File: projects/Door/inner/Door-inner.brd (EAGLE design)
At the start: 80 x 53.3 mm, 28 parts, among them IC1 7815TV, J2 AVR_SPI_PROG_3X2PTH, J3 LCD, U2 LP2985-33DBVR, X1 POWERSUPPLY_DC21MMX, Y1 16MHz

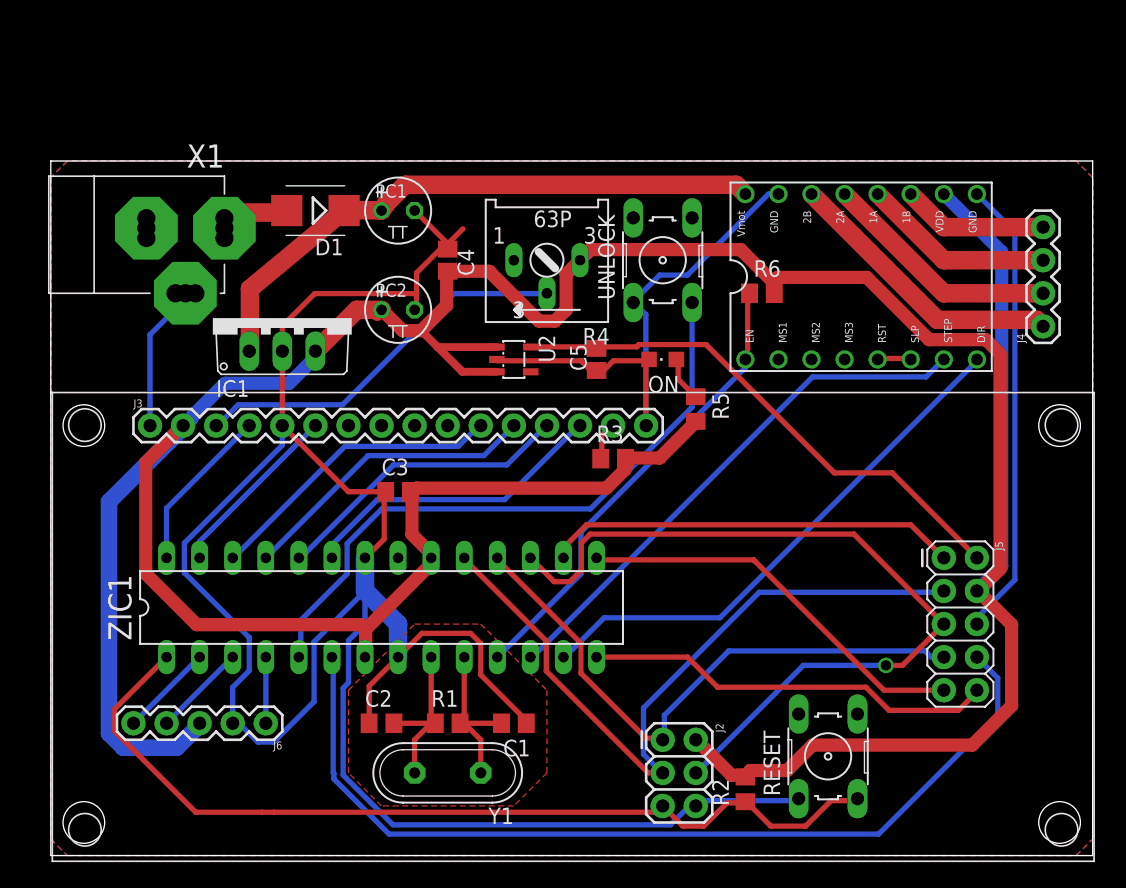
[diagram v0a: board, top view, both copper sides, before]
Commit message: Rerouted door boards for rivet-plated vias instead of plated through-holes
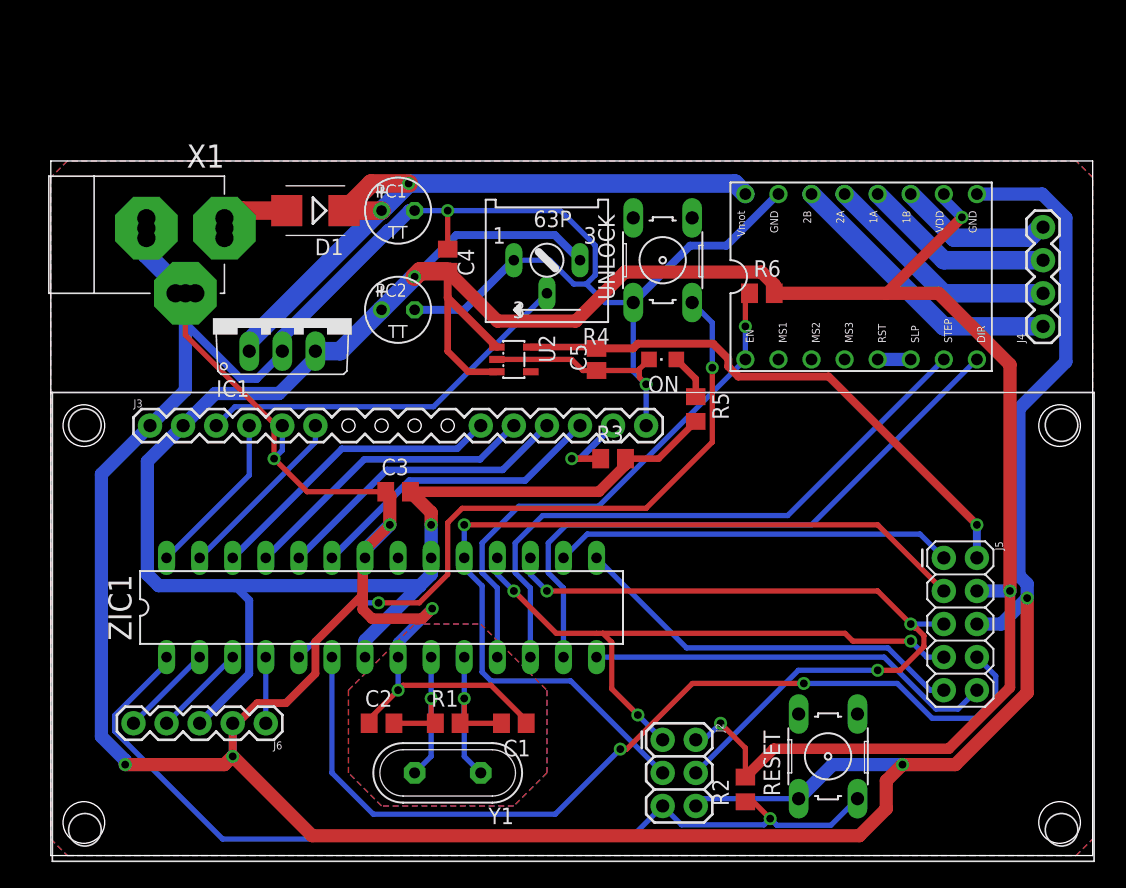
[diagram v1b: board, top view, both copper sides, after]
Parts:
- J3: value LCD -> LCD_4PINNOPADS; device lcd:LCD-16X2 -> lcd:LCD-16X2-NOPADS
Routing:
- net GND: track 264.0 -> 388.1 mm, vias 0 -> 10
- net +5V: track 289.1 -> 260.7 mm, vias 0 -> 5
- net SCK: track 55.9 -> 67.9 mm, vias 0 -> 1
- net M-STP: track 41.2 -> 48.0 mm
- net M-DIR: track 41.3 -> 48.0 mm
- net VIN: track 46.2 -> 52.9 mm, vias 0 -> 1
- net MOSI: track 64.0 -> 58.4 mm, vias 1 -> 3
- net M-EN: track 36.0 -> 40.5 mm, vias 0 -> 1
- net N$4: track 3.29 -> 6.45 mm, vias 0 -> 1
- net N$12: track 49.2 -> 52.3 mm, vias 0 -> 2
- net RESET: track 70.3 -> 73.2 mm, vias 0 -> 1
- net MISO: track 45.6 -> 48.3 mm, vias 0 -> 3
- net XTAL2: track 12.7 -> 14.6 mm, vias 0 -> 1
- net XTAL1: track 12.7 -> 14.6 mm, vias 0 -> 1
- net +3V3: track 41.3 -> 43.1 mm, vias 0 -> 1
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
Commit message: Via rivets apparently have a 0.6mm INNER diameter
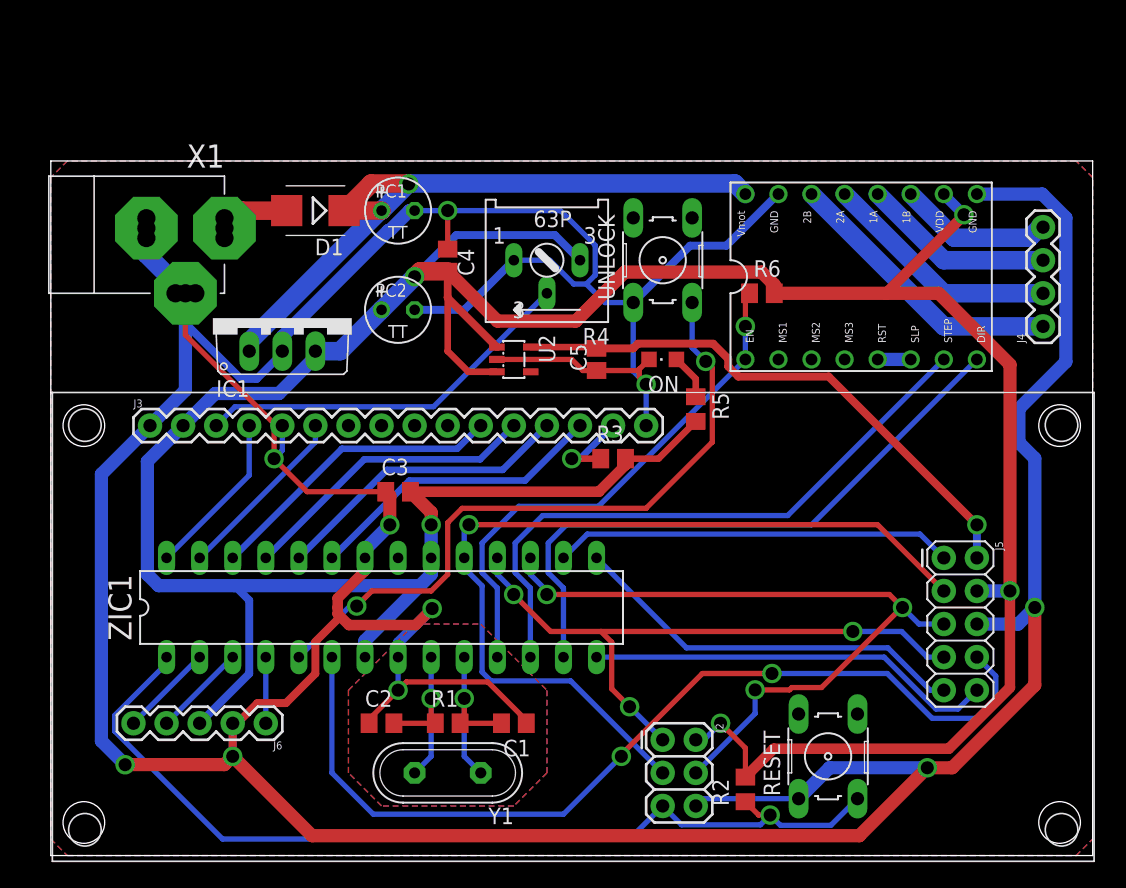
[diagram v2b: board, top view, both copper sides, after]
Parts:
- J3: value LCD_4PINNOPADS -> LCD_4PIN; device lcd:LCD-16X2-NOPADS -> lcd:LCD-16X2
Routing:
- net MOSI: track 58.4 -> 57.0 mm
- net STATUS: track 70.8 -> 71.6 mm

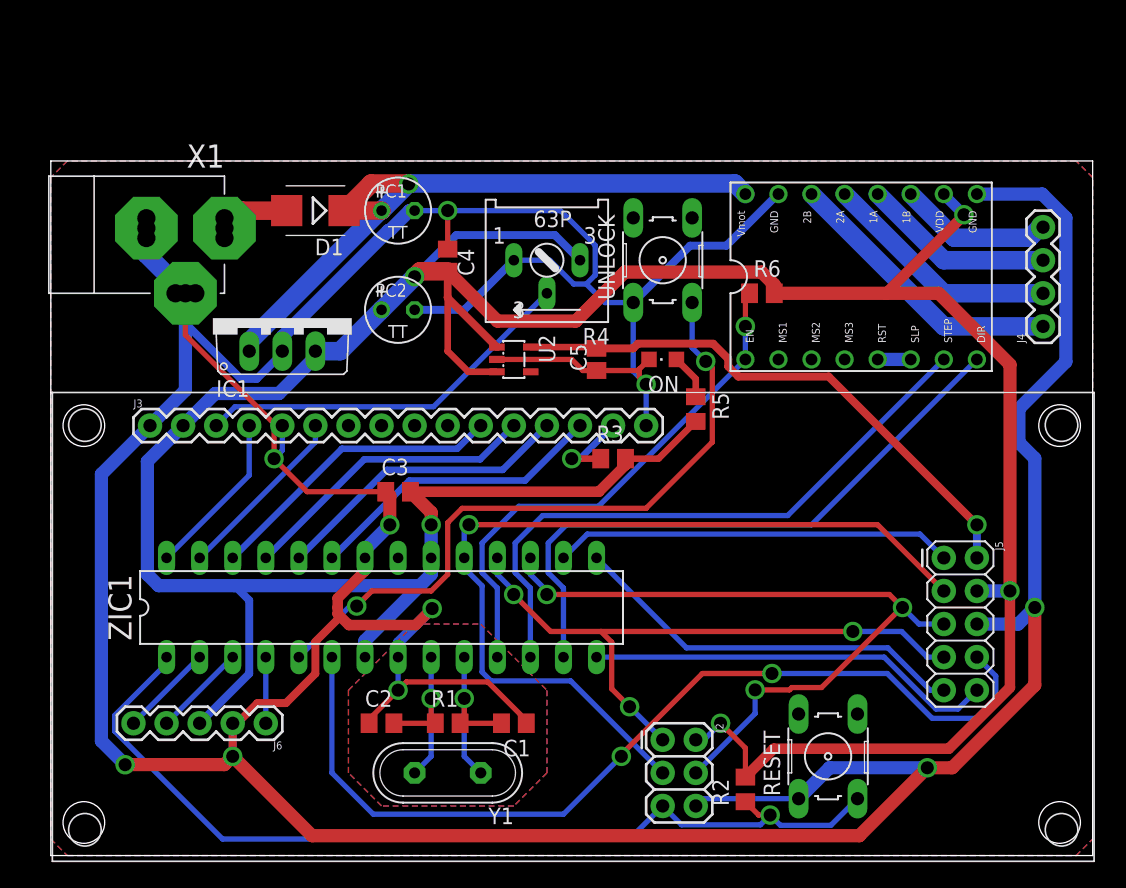
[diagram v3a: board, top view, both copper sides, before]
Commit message: Door-inner redesign
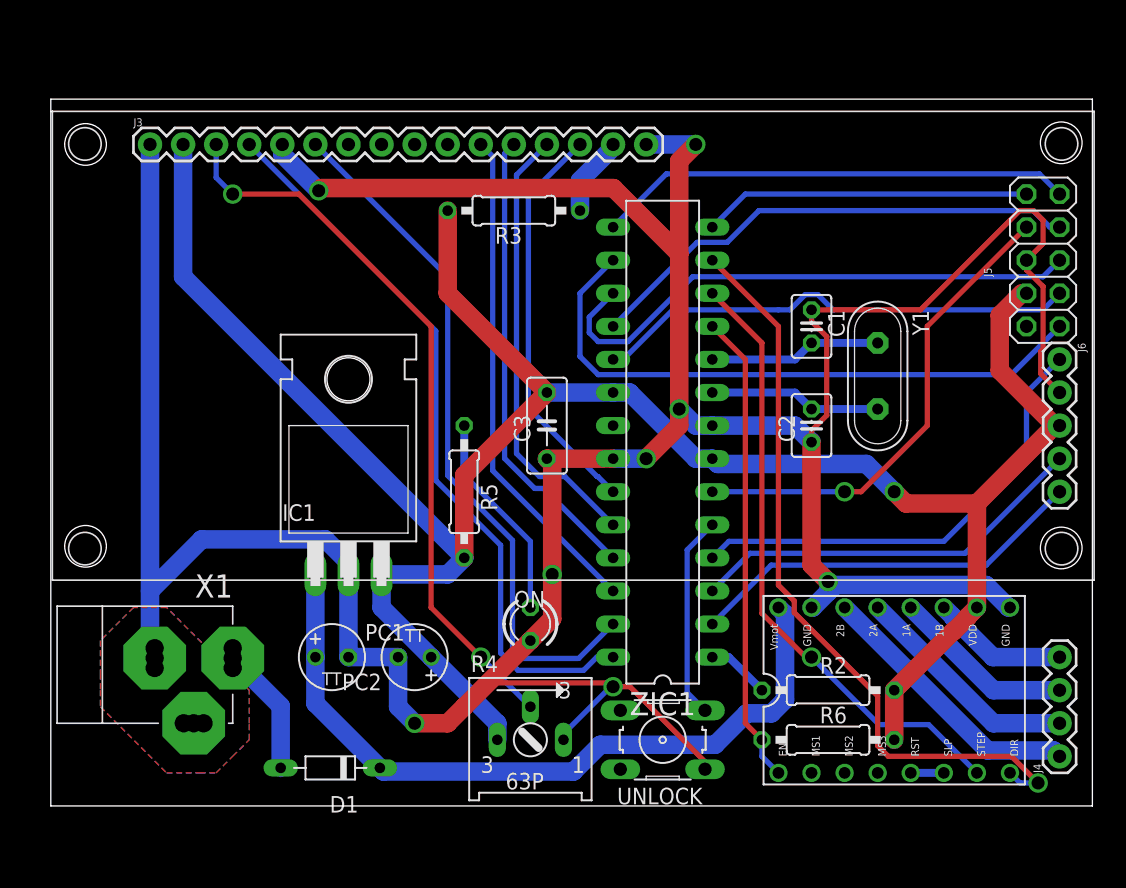
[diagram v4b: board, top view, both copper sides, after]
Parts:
- removed C4: 100n, SmartPrj:C0805
- removed C5: 1u, SmartPrj:C0805
- removed J2: AVR_SPI_PROG_3X2PTH, SparkFun-Connectors:2X3
- removed R1: 1M, resistor:R0805
- removed RESET: (no value), switch-omron:B3F-10XX
- removed U2: LP2985-33DBVR, texas:SOT23-DBV
- C1, C2: device resistor:C0805 -> resistor:C025-030X050
- C3: device resistor:C0805 -> resistor:C050-030X075
- D1: device diode:SMB -> diode:D-7.5
- IC1: value 7815TV -> 7815T; device linear:TO220V -> linear:TO220H
- J5: device SparkFun-Connectors:2X5 -> pinhead:2X05
- ON: device led:CHIPLED_0805 -> led:LED3MM
- R2, R3, R5, R6: device resistor:R0805 -> resistor:0207/10
- moved J6 67.1 mm to (77.5, 31.8), turned to 270 degrees
- moved Y1 44.9 mm to (63.5, 30.5), turned to 270 degrees
- moved D1 42.8 mm to (21.5, 0.38)
- moved C2 40.2 mm to (58.4, 26.7), turned to 90 degrees
- moved C1 38.1 mm to (58.4, 34.3), turned to 270 degrees
- moved R4 36.9 mm to (36.8, 2.54), turned to 0 degrees
- moved UNLOCK 36.8 mm to (47.0, 2.54), turned to 180 degrees
- moved PC1 34.7 mm to (21.6, 8.89)
- moved R6 34.7 mm to (59.7, 2.54)
- moved J4 33.0 mm to (77.5, 1.27)
- moved X1 33.0 mm to (7.62, 8.89)
- moved U$1 31.9 mm to (57.1, 11.4)
- moved PC2 26.7 mm to (27.9, 8.89), turned to 180 degrees
- moved ZIC1 25.0 mm to (47.0, 25.4), turned to 90 degrees
- moved J5 24.1 mm to (76.2, 39.4), turned to 90 degrees
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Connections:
- net +3V3: no longer C5.2, U2.5
- net +5V: no longer C4.2, J2.2, U2.1, U2.3
- net GND: now also ON.K; no longer C4.1, C5.1, J2.6, ON.C, RESET.1, U2.2
- net MISO: no longer J2.1
- net MOSI: no longer J2.4
- net RESET: no longer J2.5, RESET.3
- net SCK: no longer J2.3
- net XTAL1: no longer R1.1
- net XTAL2: no longer R1.2
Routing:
- net GND: track 387.9 -> 293.0 mm, vias 10 -> 8
- net +5V: track 260.8 -> 175.2 mm, vias 5 -> 1
- net RESET: track 73.3 -> 4.86 mm, vias 1 -> 0
- net LCD-RS: track 12.8 -> 56.7 mm
- net +3V3: track 43.1 -> 0.00 mm, vias 1 -> 0
- net LCD-EN: track 13.8 -> 54.1 mm
- net N$12: track 52.3 -> 15.6 mm, vias 2 -> 0
- net STATUS: track 71.6 -> 37.0 mm, vias 2 -> 1
- net N$1: track 5.08 -> 36.0 mm
- net SCK: track 67.7 -> 37.4 mm, vias 1 -> 0
- net N$5: track 29.6 -> 56.2 mm, vias 0 -> 2
- net N$3: track 7.18 -> 30.9 mm
- net N$2: track 7.18 -> 30.9 mm
- net SDA: track 30.7 -> 47.4 mm
- net D4: track 23.3 -> 38.5 mm
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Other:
- board size 80 x 53.3 mm -> 80 x 54.3 mm

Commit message: Inner door modifications
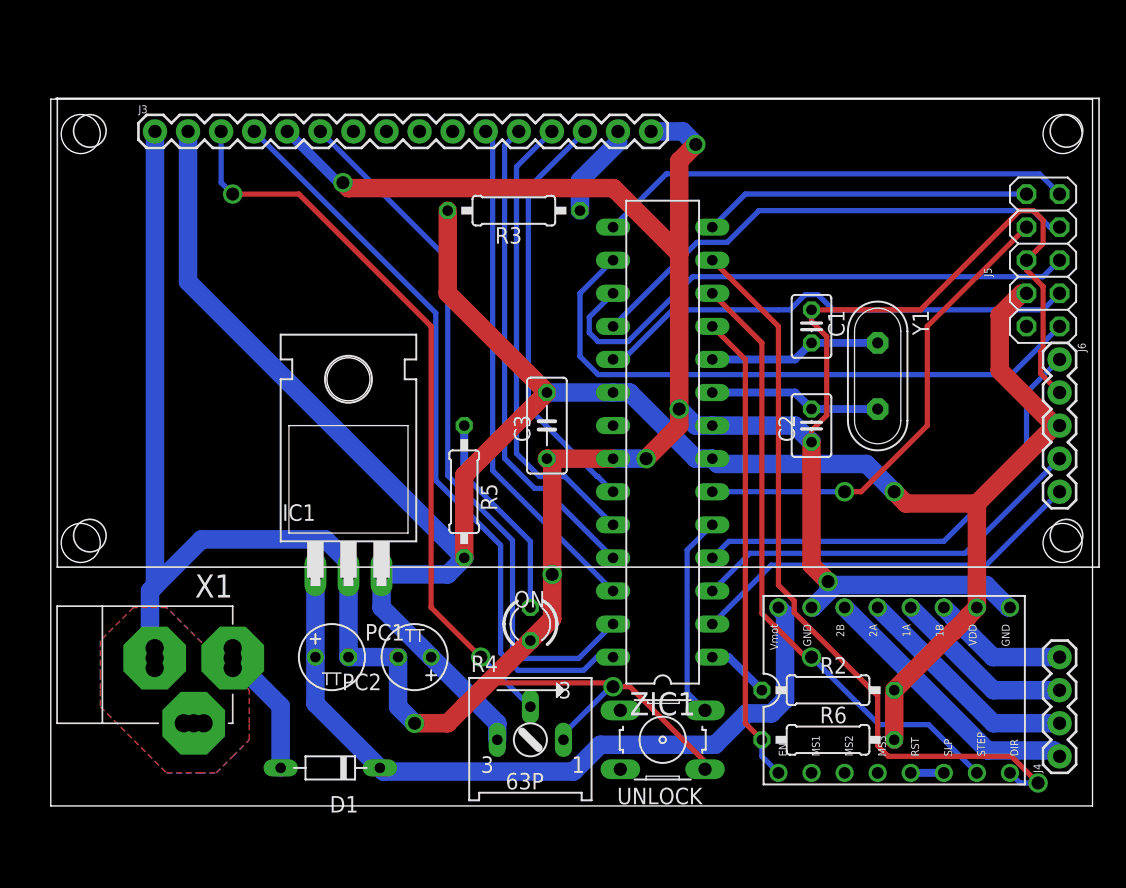
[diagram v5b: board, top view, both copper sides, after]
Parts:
- moved J3 1.07 mm to (8.00, 49.3)
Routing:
- net N$4: track 6.13 -> 7.29 mm
- net D5: track 35.9 -> 37.1 mm
- net D7: track 31.0 -> 32.2 mm
- net D6: track 34.4 -> 35.5 mm
- net +5V: track 175.2 -> 176.0 mm
- net LCD-RS: track 56.7 -> 57.5 mm
- net D4: track 38.5 -> 39.3 mm
- net N$5: track 56.2 -> 57.0 mm
- net LCD-EN: track 54.1 -> 54.9 mm

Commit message: Extra vias in inner door
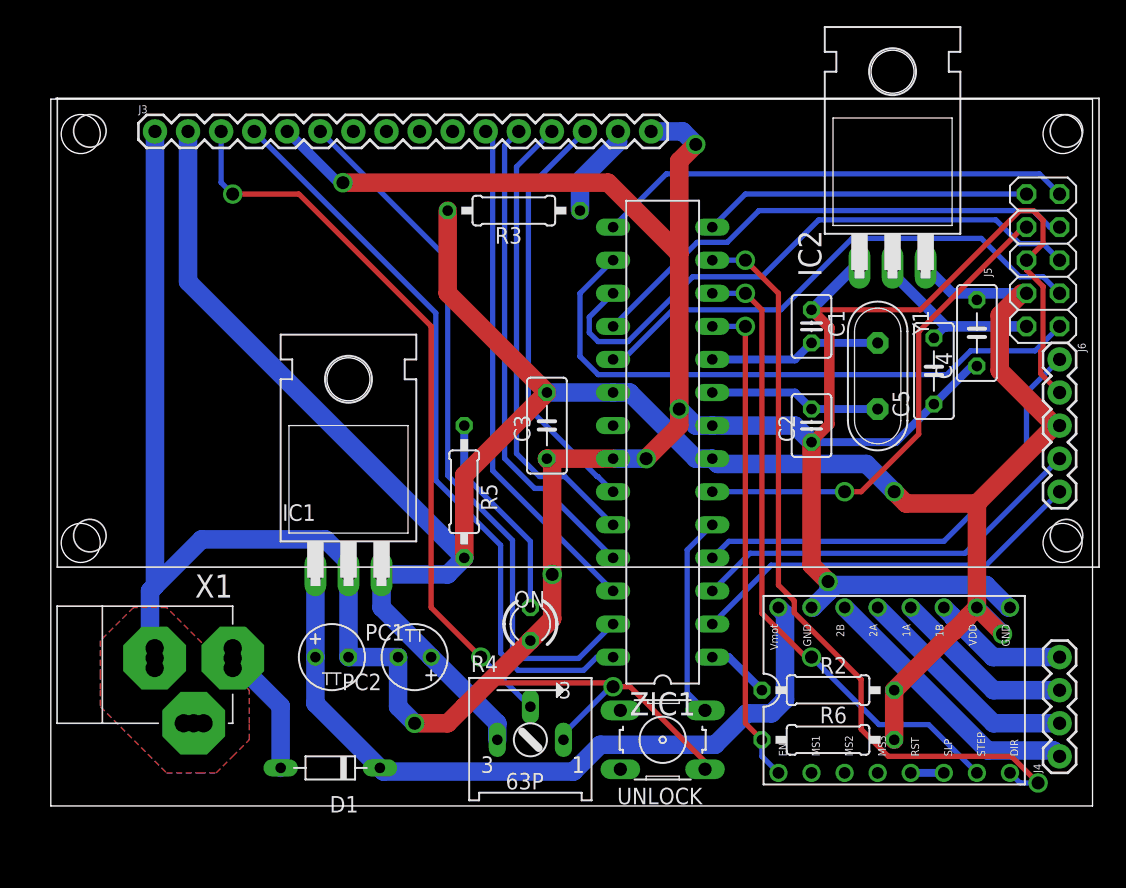
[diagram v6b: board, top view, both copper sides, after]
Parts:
- added C4: 100n, resistor:C050-030X075
- added C5: 1u, resistor:C050-030X075
- added IC2: 317T, linear:TO220H
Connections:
- net +3V3: now also C5.2, IC2.2
- net +5V: now also C4.2, IC2.3
- net GND: now also C4.1, C5.1, IC2.1
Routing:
- net GND: track 293.1 -> 313.5 mm
- net +5V: track 176.0 -> 190.9 mm, vias 1 -> 2
- net +3V3: track 0.00 -> 13.7 mm
- net MOSI: track 42.8 -> 45.3 mm
- net SCK: track 37.4 -> 39.9 mm
- net M-DIR: track 58.5 -> 60.0 mm, vias 1 -> 2
- net M-STP: track 47.7 -> 49.2 mm, vias 1 -> 2
- net M-EN: track 36.4 -> 37.9 mm, vias 0 -> 1
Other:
- board text added: "Door Rev. 1.2.0"

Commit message: New door, for making with plated through-holes
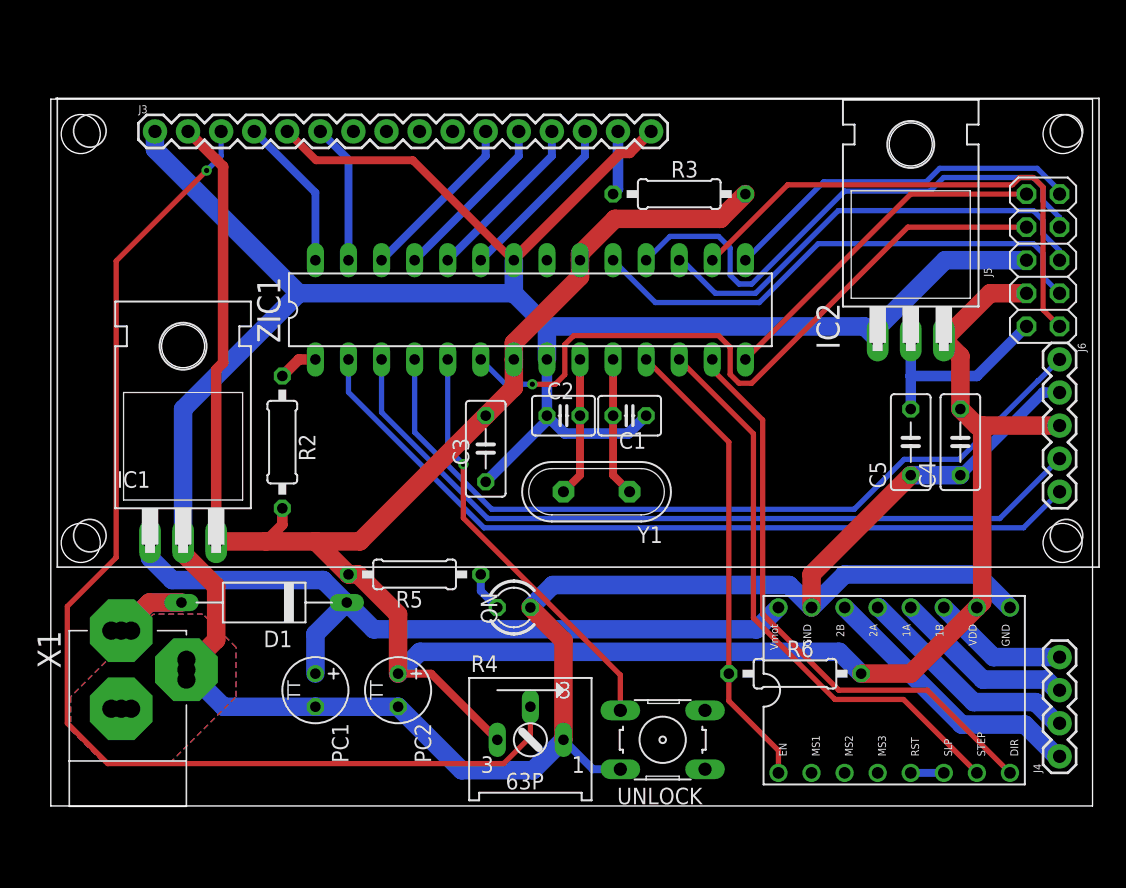
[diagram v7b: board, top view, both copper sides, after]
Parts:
- D1: device diode:D-7.5 -> diode:D-12.5
- moved R2 46.0 mm to (17.8, 25.4), turned to 270 degrees
- moved Y1 23.3 mm to (41.9, 21.6), turned to 180 degrees
- moved C2 19.1 mm to (39.4, 27.4), turned to 0 degrees
- moved C1 15.6 mm to (44.5, 27.4), turned to 180 degrees
- moved ZIC1 14.4 mm to (36.8, 35.6), turned to 0 degrees
- moved D1 13.7 mm to (16.4, 13.1)
- moved IC1 13.0 mm to (10.2, 27.9)
- moved R3 12.8 mm to (48.3, 44.5), turned to 0 degrees
- moved C4 8.48 mm to (69.8, 25.4)
- moved R5 7.41 mm to (27.9, 15.2), turned to 180 degrees
- moved IC2 5.76 mm to (66.0, 43.4)
- moved C5 5.74 mm to (66.0, 25.4)
- moved R6 5.68 mm to (57.1, 7.62)
- moved C3 5.02 mm to (33.4, 24.9)
- moved X1 4.89 mm to (5.33, 4.57), turned to 180 degrees
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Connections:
- net GND: now also UNLOCK.2; no longer UNLOCK.1
- net N$12: now also UNLOCK.4; no longer UNLOCK.3
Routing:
- net LCD-RS: track 57.5 -> 11.8 mm
- net LCD-EN: track 54.9 -> 10.8 mm
- net N$5: track 57.0 -> 90.3 mm, vias 2 -> 1
- net N$3: track 30.9 -> 62.6 mm
- net N$2: track 30.9 -> 61.4 mm
- net N$1: track 36.0 -> 62.3 mm
- net D4: track 39.3 -> 13.2 mm
- net D5: track 37.1 -> 13.2 mm
- net GND: track 313.5 -> 290.7 mm, vias 8 -> 0
- net D6: track 35.5 -> 13.2 mm
- net D7: track 32.2 -> 13.2 mm
- net N$12: track 15.6 -> 32.4 mm, vias 0 -> 1
- net STATUS: track 37.2 -> 53.3 mm
- net M-DIR: track 60.0 -> 45.2 mm, vias 2 -> 0
- net N$6: track 16.1 -> 3.07 mm
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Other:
- board text added: "Door Rev. 1.3.0"
- board text removed: "Door Rev. 1.2.0"
